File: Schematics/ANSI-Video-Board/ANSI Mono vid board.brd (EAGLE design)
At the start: 121.6 x 88.9 mm, 25 parts, among them IC1 74HCT166N, Q1 16MHz, U1 ATMEGA328P

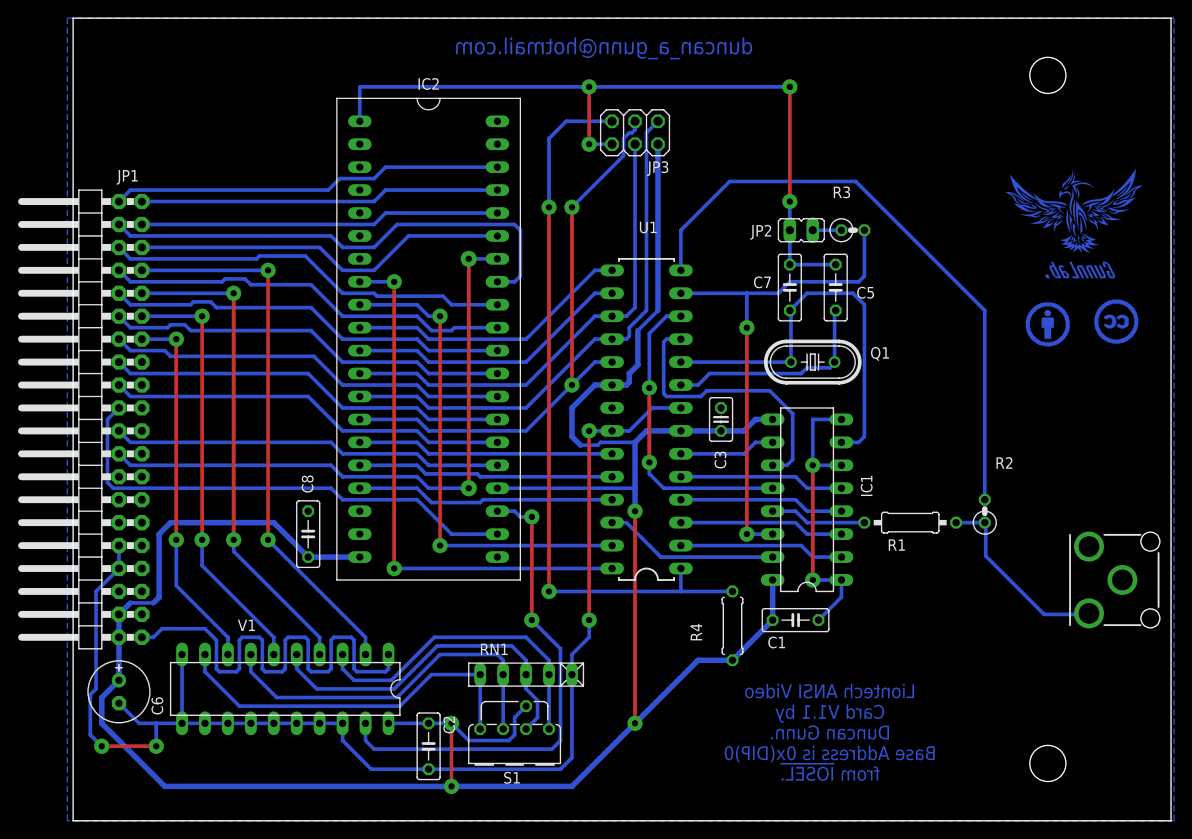
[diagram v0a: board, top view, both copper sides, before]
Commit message: Updated to have a formal Timer IRQ.  Currently this is T1 on the W65C22 on the GPIO card, so if you want to use it that card must be present.
The prebuilt ROM ToEVID.bin uses this card at 0xC040.

A couple of minor whoopsies have been fixed as well.
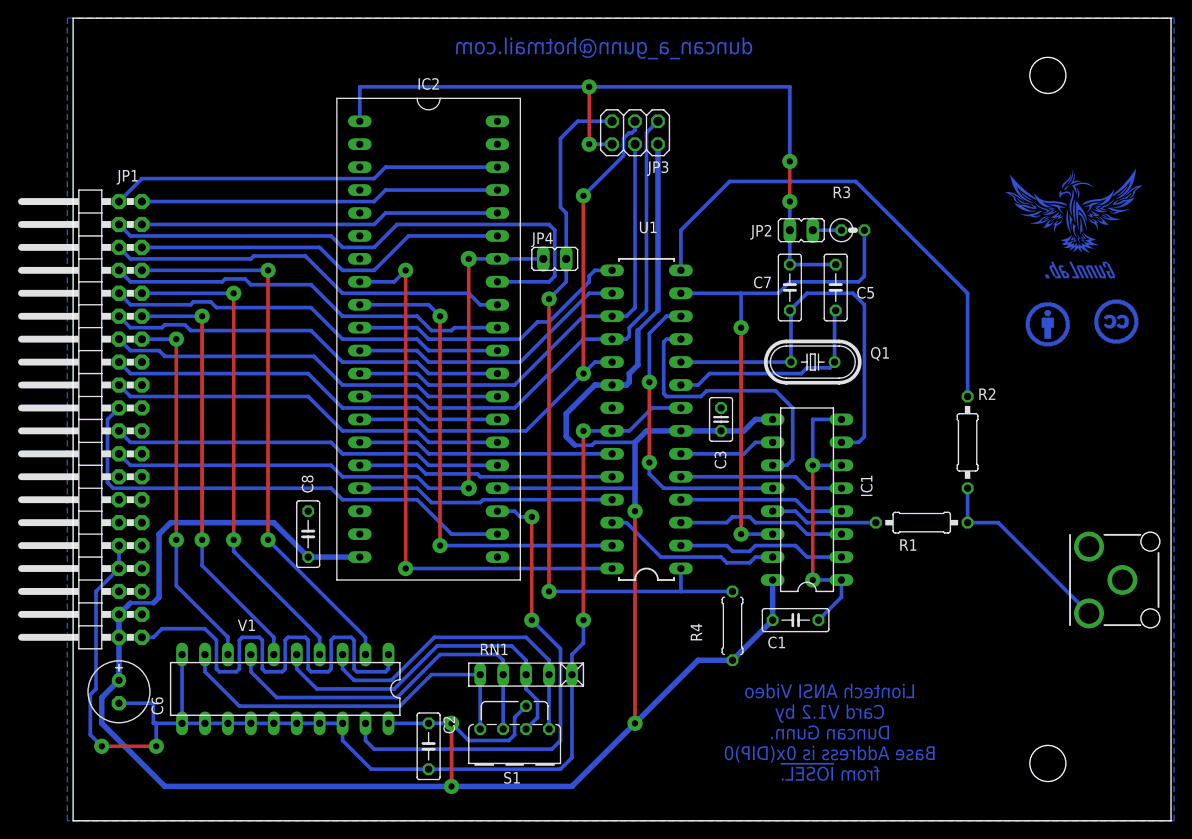
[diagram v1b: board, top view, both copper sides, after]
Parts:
- added JP4: (no value), jumper:JP1
- R2: device rcl:0207/2V -> rcl:0207/10
- moved R2 7.85 mm to (99.1, 41.9)
- moved R1 1.27 mm to (94.0, 33.0)
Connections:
- net !AVR_RST: now also JP4.2
- net RESB: now also JP4.1
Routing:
- net N$13: track 67.2 -> 55.0 mm
- net D0: track 54.7 -> 62.3 mm
- net RESB: track 68.9 -> 74.0 mm
- net DD4-SCK: track 63.9 -> 62.1 mm
- net AVAIL: track 59.7 -> 61.5 mm
- net GND: track 261.2 -> 262.9 mm
- net N$12: track 10.7 -> 12.0 mm
- net VCC: track 272.9 -> 273.8 mm
- net N$16: track 21.1 -> 21.9 mm
- net N$11: track 55.7 -> 56.4 mm
- net N$4: track 18.3 -> 18.8 mm
- net N$14: track 19.4 -> 19.9 mm
- net N$5: track 18.3 -> 18.8 mm
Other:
- board text added: "Liontech ANSI Video Card V1.2 by Duncan Gunn. Base Address is 0x(DIP)0 from !IOSEL."
- board text removed: "Liontech ANSI Video Card V1.1 by Duncan Gunn. Base Address is 0x(DIP)0 from !IOSEL."
